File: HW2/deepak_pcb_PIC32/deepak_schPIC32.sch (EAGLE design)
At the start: 3 parts

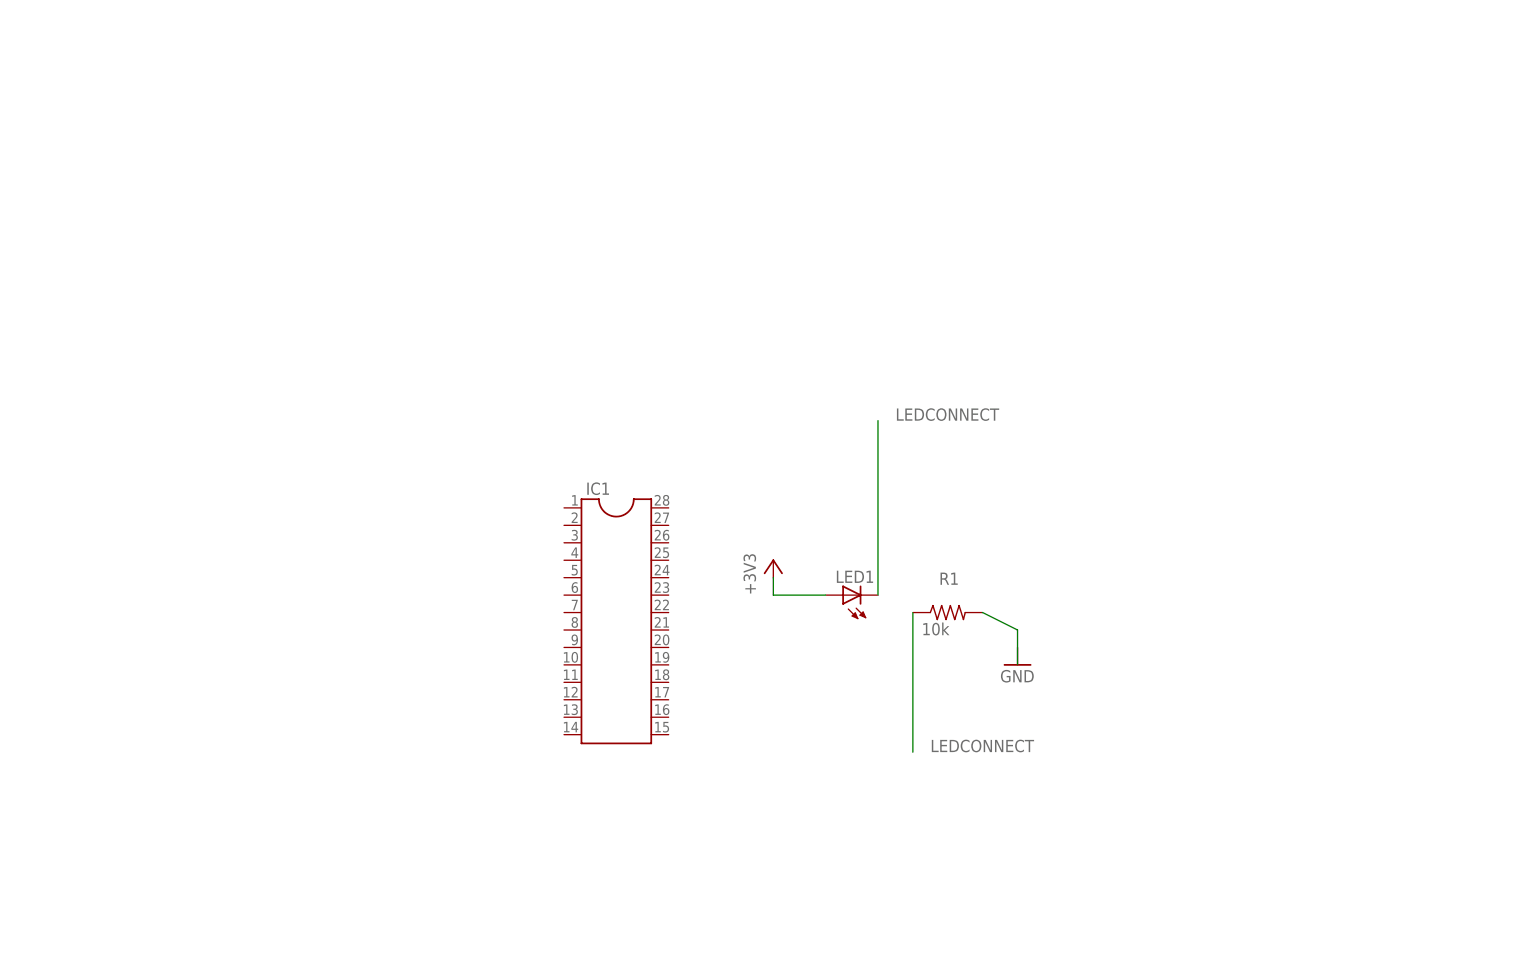
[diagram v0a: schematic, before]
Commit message: First pass at schematic. Push buttons and side switch left
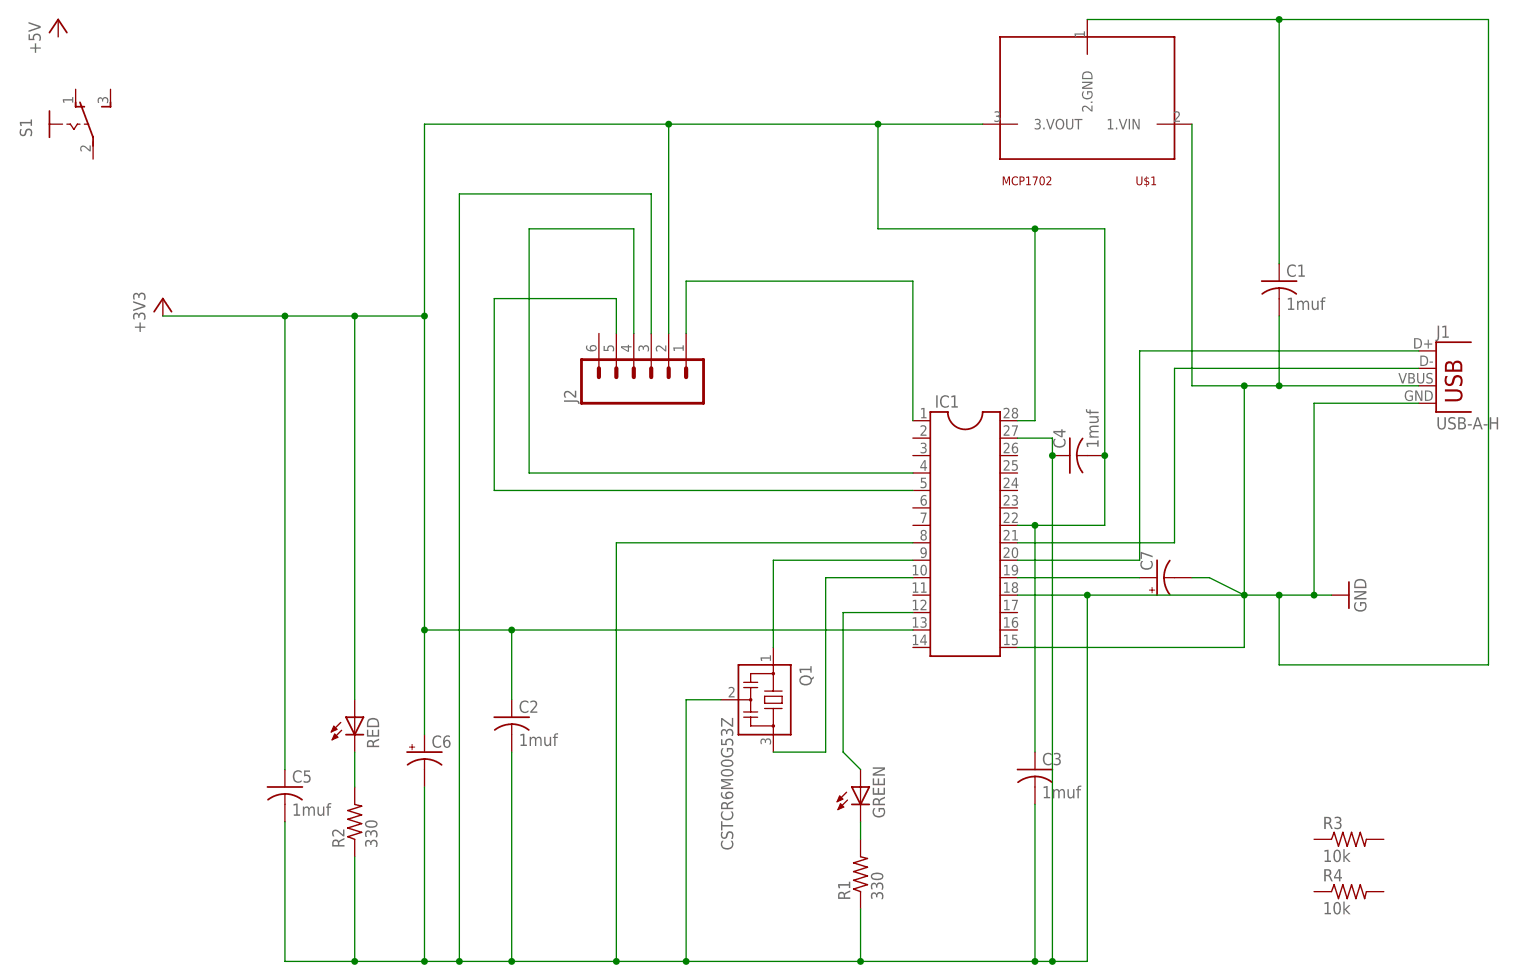
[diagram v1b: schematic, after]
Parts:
- removed LED1: (no value), led:LED3MM
- added C1, C2, C3, C4, C5: 1muf, ME433:C-US025-025X050
- added C6, C7: (no value), ME433:CPOL-USE2-4
- added GREEN, RED: (no value), ME433:LED3MM
- added J1: USB-A-H, ME433:USB-A-H
- added J2: (no value), ME433:M06SMD_MALE
- added Q1: CSTCR6M00G53Z, murata-filter:CSTCR6M00G53Z
- added R2: 330, ME433:R-US_0207/10
- added R3, R4: 10k, ME433:R-US_0207/10
- added S1: (no value), switch:255SB
- added U$1: MCP1702, ME433:MCP1702
- R1: value 10k -> 330; device resistor:R-US_0207/10 -> ME433:R-US_0207/10
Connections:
- removed net LEDCONNECT: LED1.C, R1.1
- new net GND: C1.1, C2.2, C3.2, C4.1, C5.2, C6.-, C7.-, IC1.18, IC1.27, IC1.8, J1.GND, J2.3, Q1.2, R1.1, R2.1, U$1.2.GND
- new net N$1: C1.2, IC1.15, J1.VBUS, U$1.1.VIN
- new net N$10: GREEN.C, R1.2
- new net N$11: C7.+, IC1.19
- new net N$12: IC1.21, J1.D-
- new net N$3: IC1.1, J2.1
- new net N$4: IC1.9, Q1.1
- new net N$5: IC1.10, Q1.3
- new net N$6: IC1.4, J2.4
- new net N$7: IC1.5, J2.5
- new net N$8: IC1.20, J1.D+
- new net N$9: GREEN.A, IC1.12
- net +3V3: now also C2.1, C3.1, C4.2, C5.1, C6.+, IC1.13, IC1.22, IC1.28, J2.2, RED.A, U$1.3.VOUT; no longer LED1.A
- net N$2: now also R2.2, RED.C; no longer R1.2
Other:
- moved on the sheet: IC1, R1

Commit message: Second attempt at schematic
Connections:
- new net +5V: S1.S, U$1.1.VIN
- net N$1: now also S1.P; no longer U$1.1.VIN
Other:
- moved on the sheet: S1
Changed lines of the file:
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@@
 <instance part="R4" gate="G$1" x="132.08" y="10.16"/>
 <instance part="U$1" gate="G$1" x="93.98" y="121.92" rot="R180"/>
-<instance part="P+1" gate="1" x="-55.88" y="137.16"/>
+<instance part="P+1" gate="1" x="114.3" y="116.84"/>
 <instance part="+3V1" gate="G$1" x="-40.64" y="96.52"/>
 <instance part="C1" gate="G$1" x="121.92" y="99.06"/>
@@
 <instance part="C7" gate="G$1" x="104.14" y="55.88" rot="R90"/>
 <instance part="J2" gate="G$1" x="30.48" y="86.36" rot="R90"/>
-<instance part="S1" gate="1" x="-53.34" y="121.92"/>
+<instance part="S1" gate="1" x="106.68" y="104.14"/>
 </instances>
 <busses>
@@
 <net name="N$1" class="0">
 <segment>
-<pinref part="U$1" gate="G$1" pin="1.VIN"/>
-<wire x1="109.22" y1="83.82" x2="109.22" y2="121.92" width="0.1524" layer="91"/>
 <pinref part="J1" gate="G$1" pin="VBUS"/>
 <wire x1="109.22" y1="83.82" x2="116.84" y2="83.82" width="0.1524" layer="91"/>
@@
 <wire x1="116.84" y1="45.72" x2="116.84" y2="83.82" width="0.1524" layer="91"/>
 <junction x="116.84" y="83.82"/>
+<pinref part="S1" gate="1" pin="P"/>
+<wire x1="109.22" y1="99.06" x2="109.22" y2="83.82" width="0.1524" layer="91"/>
 </segment>
 </net>
@@
 </segment>
 </net>
+<net name="+5V" class="0">
+<segment>
+<pinref part="S1" gate="1" pin="S"/>
+<pinref part="P+1" gate="1" pin="+5V"/>
+<wire x1="111.76" y1="109.22" x2="114.3" y2="114.3" width="0.1524" layer="91"/>
+<pinref part="U$1" gate="G$1" pin="1.VIN"/>
+<wire x1="114.3" y1="121.92" x2="109.22" y2="121.92" width="0.1524" layer="91"/>
+<wire x1="114.3" y1="121.92" x2="114.3" y2="114.3" width="0.1524" layer="91"/>
+<junction x="114.3" y="114.3"/>
+</segment>
+</net>
